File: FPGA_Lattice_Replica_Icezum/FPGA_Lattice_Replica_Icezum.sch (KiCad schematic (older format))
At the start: 0 parts

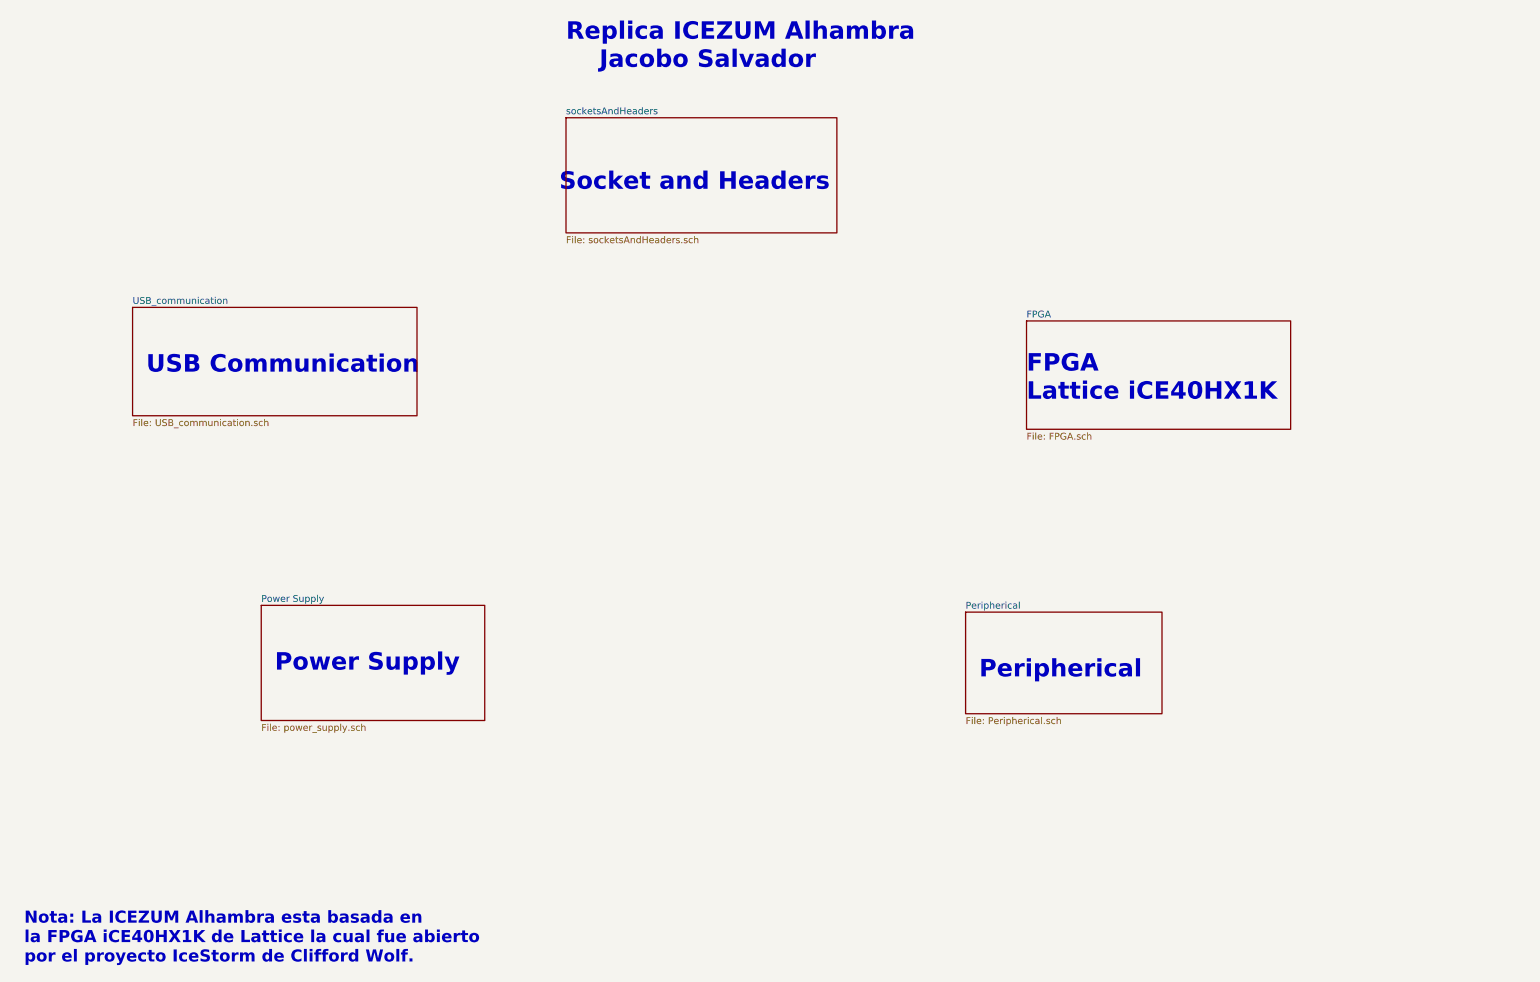
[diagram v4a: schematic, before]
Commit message: se realizo las correcciones sugeridas por el revisor
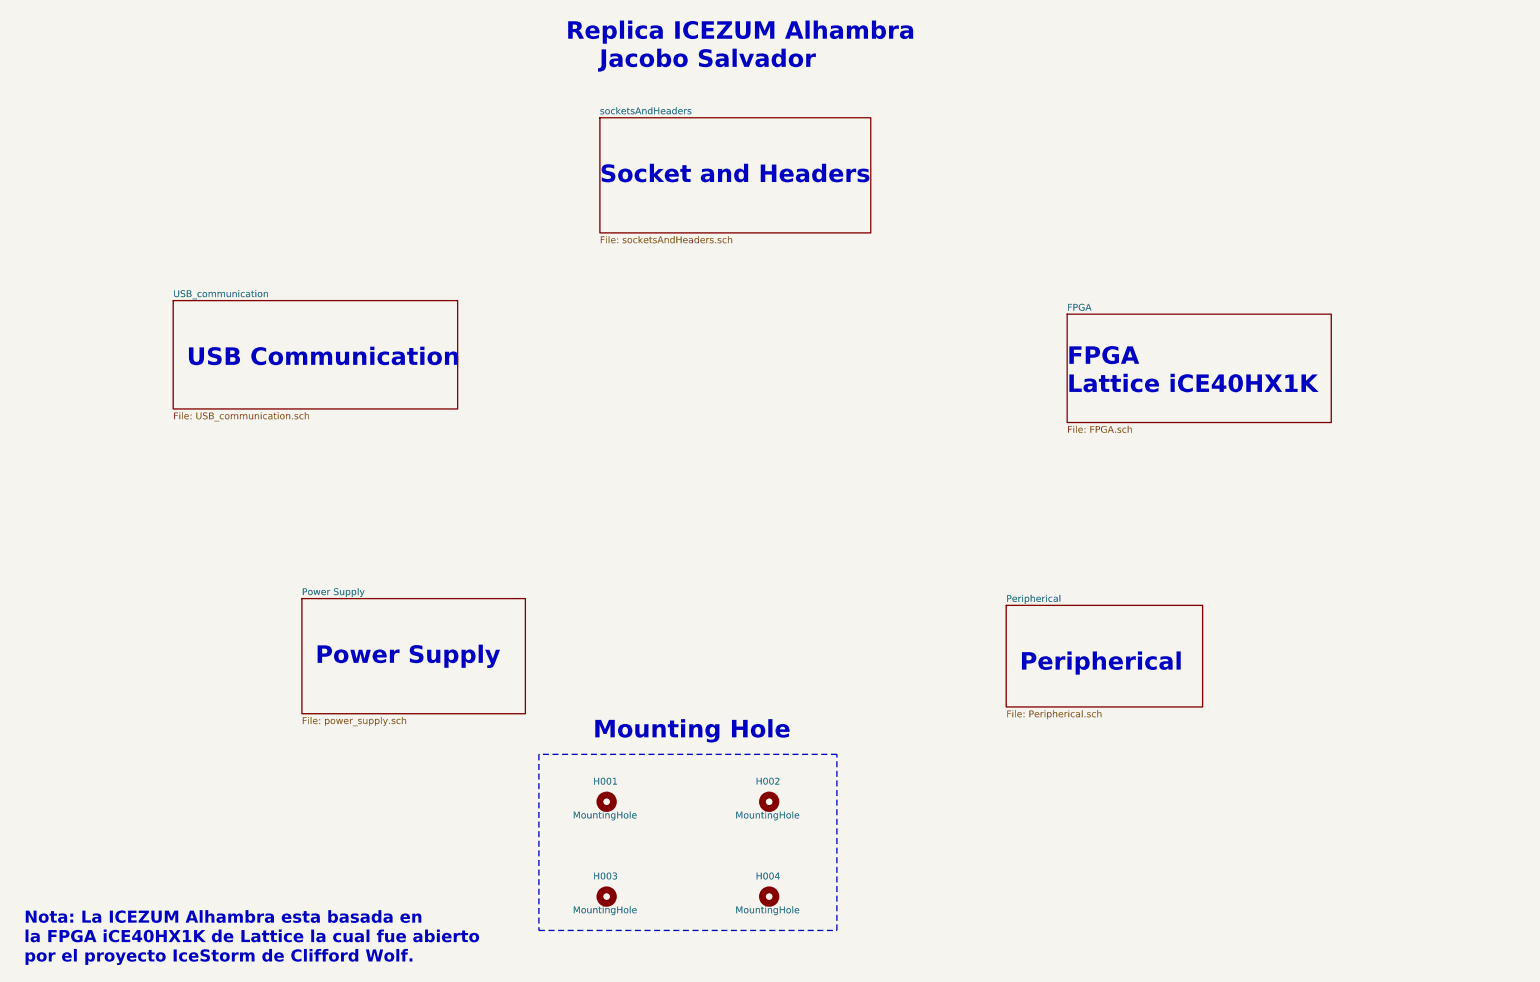
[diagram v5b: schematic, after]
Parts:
- added H001, H002, H003, H004: MountingHole, symbol Mechanical:MountingHole
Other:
- note added: "Mounting Hole"
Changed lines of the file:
@@
 $EndDescr
 $Sheet
-S 2350 5000 1650 850
+S 2650 4950 1650 850
 U 5CF4FEF6
 F0 "Power Supply" 50
@@
 $EndSheet
 $Sheet
-S 8000 2900 1950 800
+S 8300 2850 1950 800
 U 5CF846EC
 F0 "FPGA" 50
@@
 $EndSheet
 $Sheet
-S 1400 2800 2100 800
+S 1700 2750 2100 800
 U 5D2E3A88
 F0 "USB_communication" 50
@@
 $EndSheet
 $Sheet
-S 7550 5050 1450 750
+S 7850 5000 1450 750
 U 5D1D3861
 F0 "Peripherical" 50
@@
 $EndSheet
 $Sheet
-S 4600 1400 2000 850
+S 4850 1400 2000 850
 U 5CFE1C7D
 F0 "socketsAndHeaders" 50
 F1 "socketsAndHeaders.sch" 50
 $EndSheet
-Text Notes 2450 5500 0    129  ~ 26
+Text Notes 2750 5450 0    129  ~ 26
 Power Supply
-Text Notes 7650 5550 0    129  ~ 26
+Text Notes 7950 5500 0    129  ~ 26
 Peripherical\n
-Text Notes 1500 3300 0    129  ~ 26
+Text Notes 1800 3250 0    129  ~ 26
 USB Communication
-Text Notes 8000 3500 0    129  ~ 26
+Text Notes 8300 3450 0    129  ~ 26
 FPGA \nLattice iCE40HX1K
-Text Notes 4550 1950 0    129  ~ 26
+Text Notes 4850 1900 0    129  ~ 26
 Socket and Headers
 Text Notes 4600 1050 0    129  ~ 26
@@
 Text Notes 600  7650 0    89   ~ 18
 Nota: La ICEZUM Alhambra esta basada en\nla FPGA iCE40HX1K de Lattice la cual fue abierto \npor el proyecto IceStorm de Clifford Wolf.
+$Comp
+L Mechanical:MountingHole H001
+U 1 1 5D0E576C
+P 4900 6450
+F 0 "H001" H 4800 6600 50  0000 L CNN
+F 1 "MountingHole" H 4650 6350 50  0000 L CNN
+F 2 "" H 4900 6450 50  0001 C CNN
+F 3 "~" H 4900 6450 50  0001 C CNN
+	1    4900 6450
+	1    0    0    -1
+$EndComp
+$Comp
+L Mechanical:MountingHole H002
+U 1 1 5D0E5DF8
+P 6100 6450
+F 0 "H002" H 6000 6600 50  0000 L CNN
+F 1 "MountingHole" H 5850 6350 50  0000 L CNN
+F 2 "" H 6100 6450 50  0001 C CNN
+F 3 "~" H 6100 6450 50  0001 C CNN
+	1    6100 6450
+	1    0    0    -1
+$EndComp
+$Comp
+L Mechanical:MountingHole H004
+U 1 1 5D0E6006
+P 6100 7150
+F 0 "H004" H 6000 7300 50  0000 L CNN
+F 1 "MountingHole" H 5850 7050 50  0000 L CNN
+F 2 "" H 6100 7150 50  0001 C CNN
+F 3 "~" H 6100 7150 50  0001 C CNN
+	1    6100 7150
+	1    0    0    -1
+$EndComp
+$Comp
+L Mechanical:MountingHole H003
+U 1 1 5D0E62CA
+P 4900 7150
+F 0 "H003" H 4800 7300 50  0000 L CNN
+F 1 "MountingHole" H 4650 7050 50  0000 L CNN
+F 2 "" H 4900 7150 50  0001 C CNN
+F 3 "~" H 4900 7150 50  0001 C CNN
+	1    4900 7150
+	1    0    0    -1
+$EndComp
+Wire Notes Line
+	4400 6100 4400 7400
+Wire Notes Line
+	4400 7400 6600 7400
+Wire Notes Line
+	6600 7400 6600 6100
+Wire Notes Line
+	6600 6100 4400 6100
+Text Notes 4800 6000 0    129  ~ 26
+Mounting Hole
 $EndSCHEMATC

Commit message: se agregaron mas comentarios a las hojas estado del esquematico: finalizado
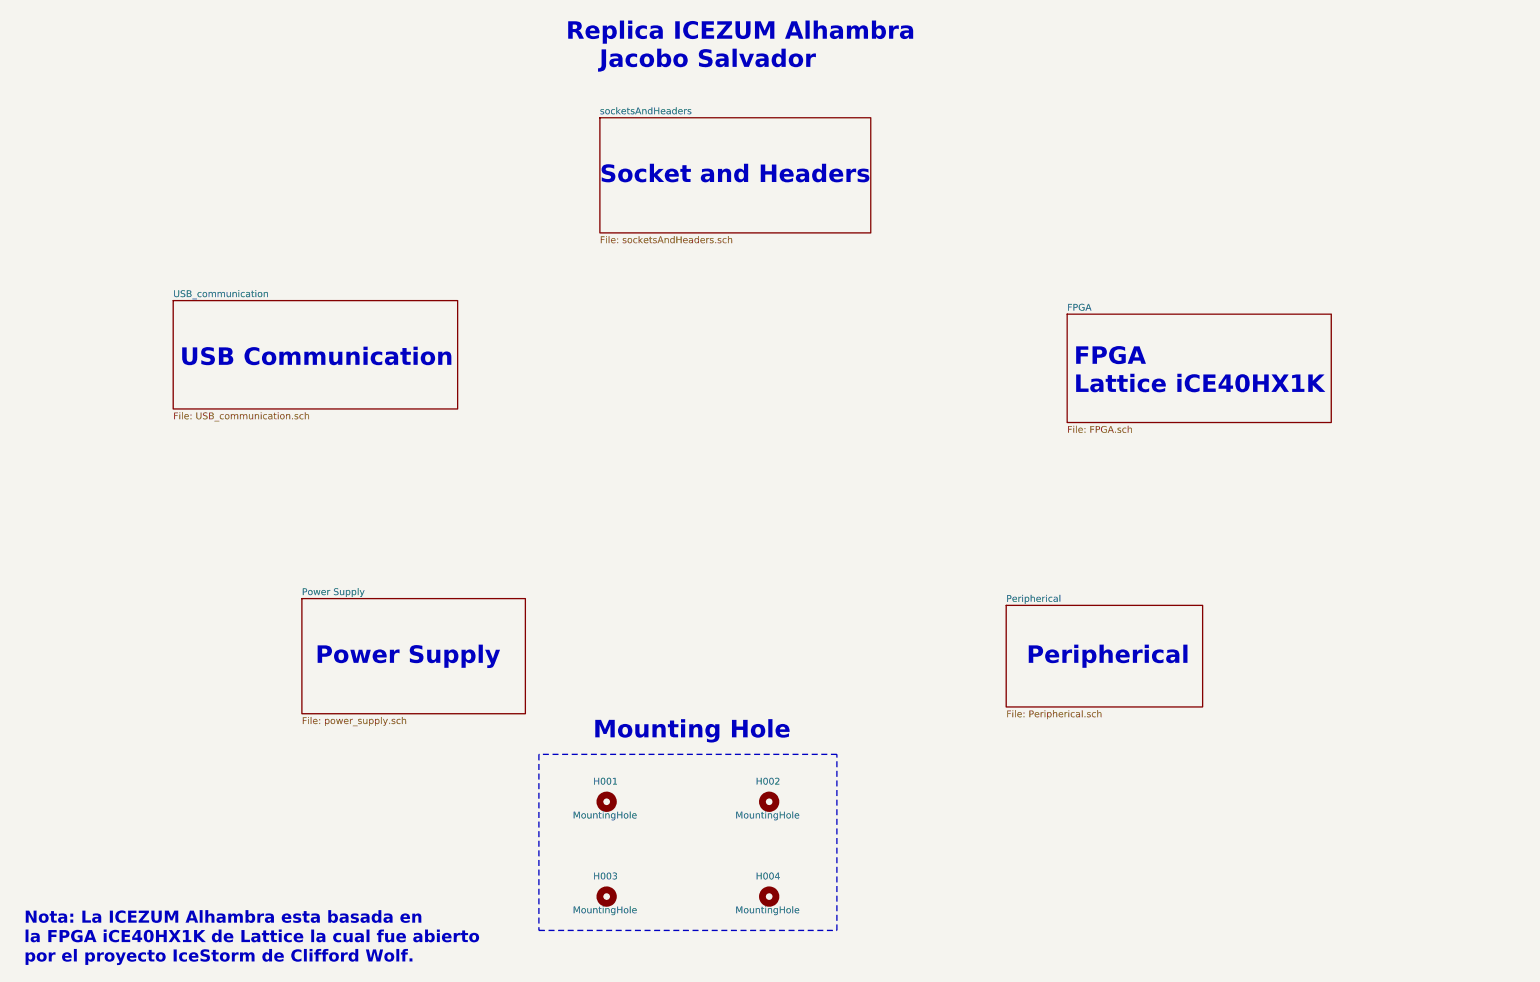
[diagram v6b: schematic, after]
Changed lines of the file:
@@
 Text Notes 2750 5450 0    129  ~ 26
 Power Supply
-Text Notes 7950 5500 0    129  ~ 26
+Text Notes 8000 5450 0    129  ~ 26
 Peripherical\n
-Text Notes 1800 3250 0    129  ~ 26
+Text Notes 1750 3250 0    129  ~ 26
 USB Communication
-Text Notes 8300 3450 0    129  ~ 26
+Text Notes 8350 3450 0    129  ~ 26
 FPGA \nLattice iCE40HX1K
 Text Notes 4850 1900 0    129  ~ 26

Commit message: se corrigieron errores de huellas y referencias que genereban errores cuando se hacia el diseño PCB
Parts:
- H001, H002, H003, H004: footprint (none) -> MountingHole:MountingHole_3.2mm_M3_ISO7380
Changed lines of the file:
@@
 F 0 "H001" H 4800 6600 50  0000 L CNN
 F 1 "MountingHole" H 4650 6350 50  0000 L CNN
-F 2 "" H 4900 6450 50  0001 C CNN
+F 2 "MountingHole:MountingHole_3.2mm_M3_ISO7380" H 4900 6450 50  0001 C CNN
 F 3 "~" H 4900 6450 50  0001 C CNN
 	1    4900 6450
@@
 F 0 "H002" H 6000 6600 50  0000 L CNN
 F 1 "MountingHole" H 5850 6350 50  0000 L CNN
-F 2 "" H 6100 6450 50  0001 C CNN
+F 2 "MountingHole:MountingHole_3.2mm_M3_ISO7380" H 6100 6450 50  0001 C CNN
 F 3 "~" H 6100 6450 50  0001 C CNN
 	1    6100 6450
@@
 F 0 "H004" H 6000 7300 50  0000 L CNN
 F 1 "MountingHole" H 5850 7050 50  0000 L CNN
-F 2 "" H 6100 7150 50  0001 C CNN
+F 2 "MountingHole:MountingHole_3.2mm_M3_ISO7380" H 6100 7150 50  0001 C CNN
 F 3 "~" H 6100 7150 50  0001 C CNN
 	1    6100 7150
@@
 F 0 "H003" H 4800 7300 50  0000 L CNN
 F 1 "MountingHole" H 4650 7050 50  0000 L CNN
-F 2 "" H 4900 7150 50  0001 C CNN
+F 2 "MountingHole:MountingHole_3.2mm_M3_ISO7380" H 4900 7150 50  0001 C CNN
 F 3 "~" H 4900 7150 50  0001 C CNN
 	1    4900 7150

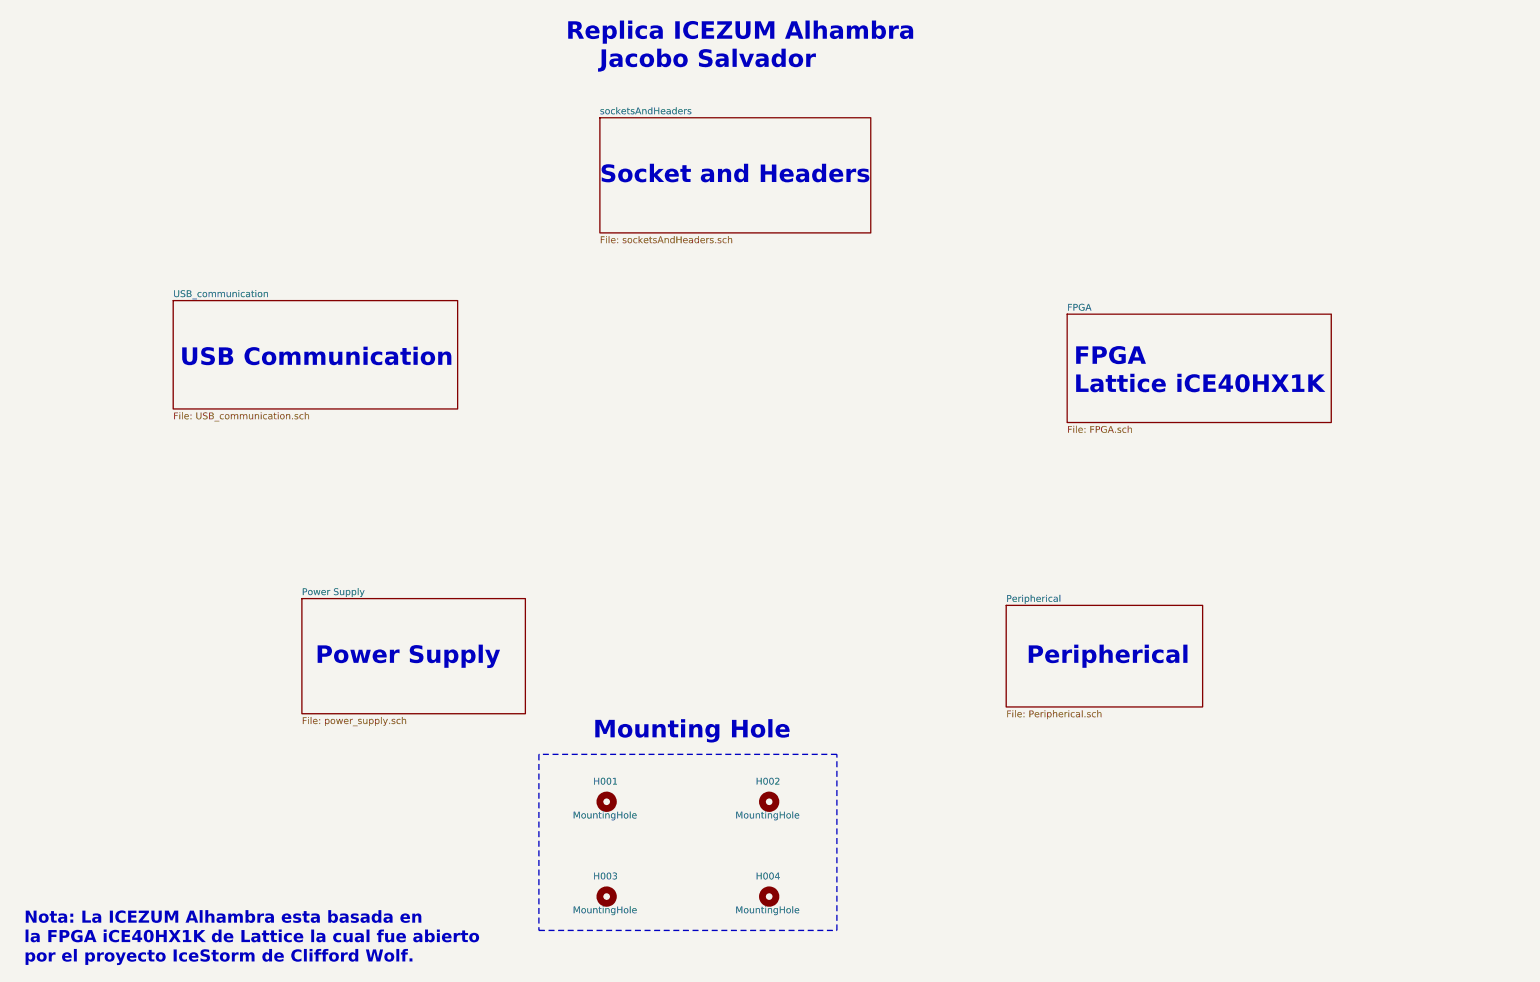
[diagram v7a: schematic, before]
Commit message: se mejoro esquematico de acuerdo a la revisión del docente. Se mejoro rotulo (se coloco link del repo, autor y autor de la versión original y la licencia) se mejoro el flujo izquiera derecha de los botones, se desplazo fiduciales a la página principal, se achico el esquematico en la parte de headers
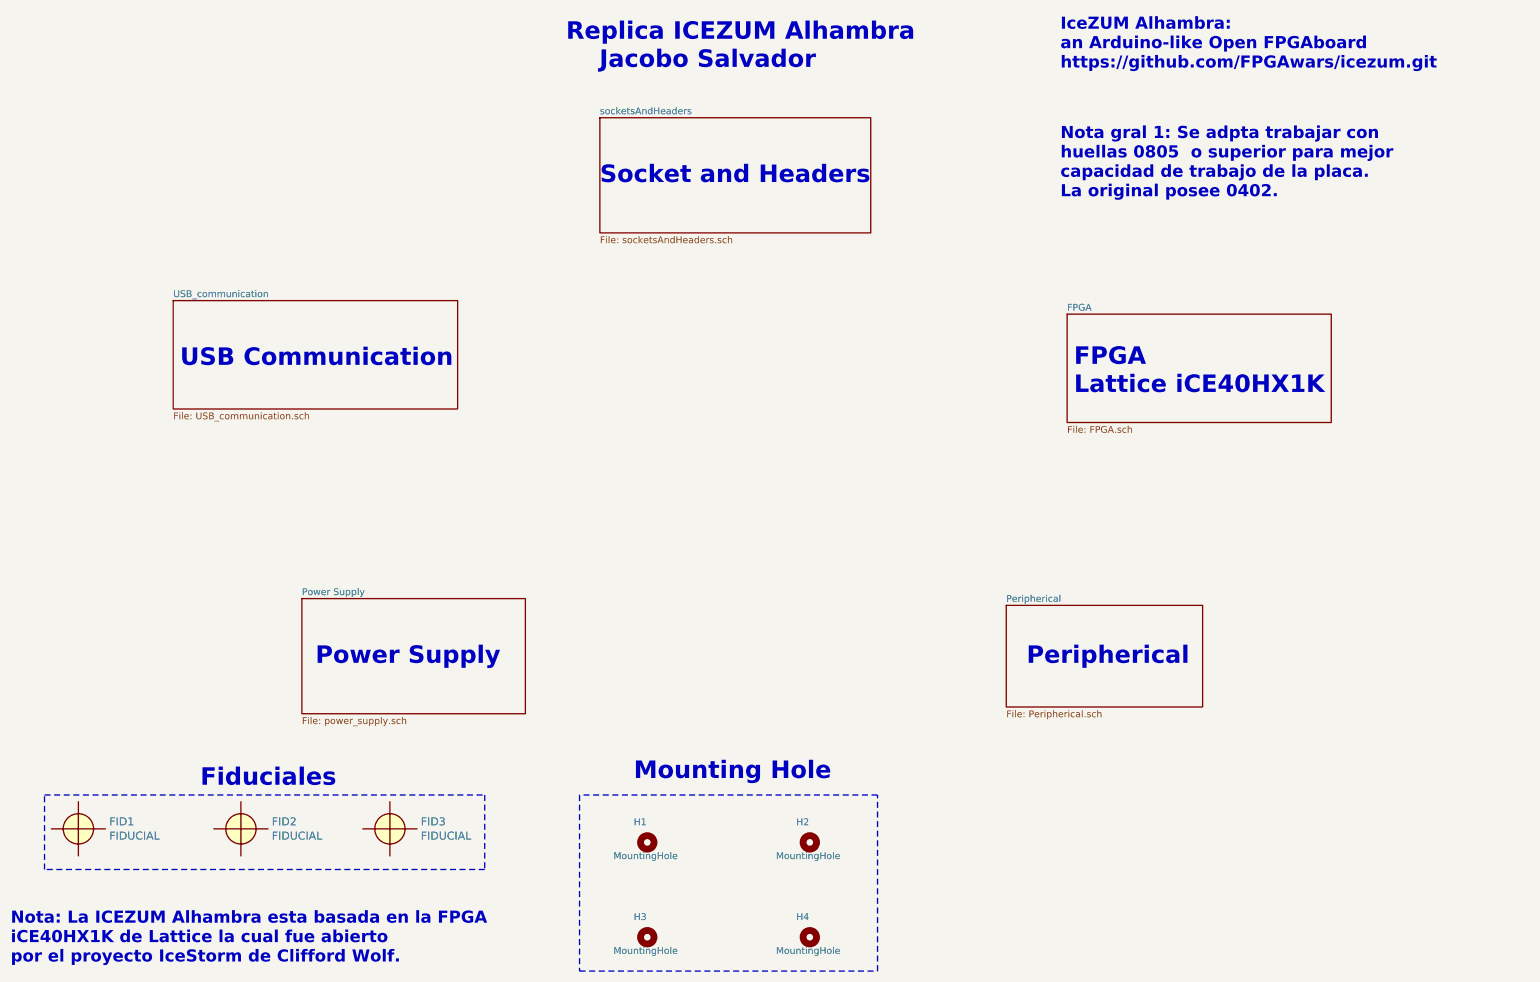
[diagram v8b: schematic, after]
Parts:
- added FID1, FID2, FID3: FIDUCIAL, footprints:Fiducial, symbol icezum:FIDUCIAL
- renumbered H001 to H1, H002 to H2, H003 to H3, H004 to H4
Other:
- note added: "Fiduciales"
- note added: "IceZUM Alhambra: \nan Arduino-like Open FPGAboard\nhttps://github.com/FPGAwars/icezum.git"
- note added: "Nota gral 1: Se adpta trabajar con \nhuellas 0805 o superior para mejor\ncapacidad de trabajo de la placa. \nLa original posee 0402."
- note added: "Nota: La ICEZUM Alhambra esta basada en la FPGA \niCE40HX1K de Lattice la cual fue abierto \npor el proyecto IceStorm de Clifford Wolf."
- note removed: "Nota: La ICEZUM Alhambra esta basada en\nla FPGA iCE40HX1K de Lattice la cual fue abierto \npor el proyecto IceStorm de Clifford Wolf."
- moved on the sheet: H1, H2, H3, H4
